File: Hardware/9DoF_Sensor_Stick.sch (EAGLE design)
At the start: 27 parts, among them U1 ITG-32001:1, U2 ADXL345, U4 3.3V

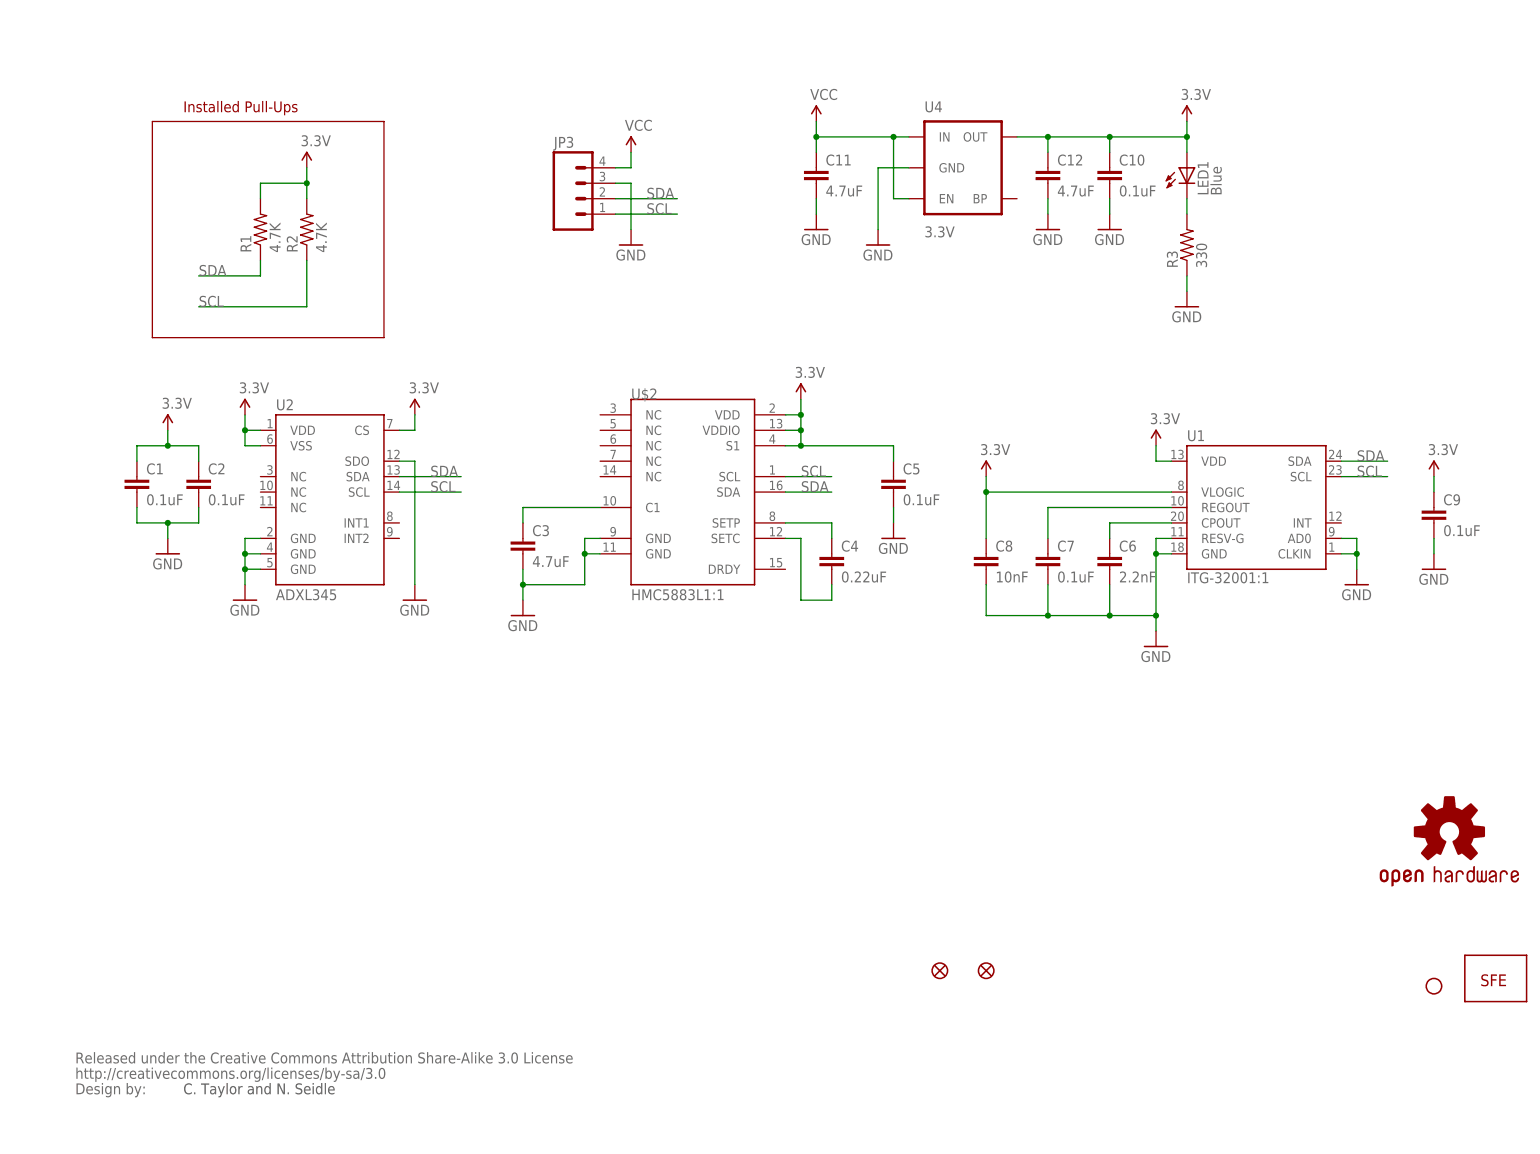
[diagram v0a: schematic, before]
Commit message: 2.0 Changes
- Replaces all three 3-axis sensors with single chip solution (LSM9DS1).
- Reduced board length from 1.3" to 1.0"
- ±2/±4/±8/±16 g linear acceleration full scale
- ±4/±8/±12/±16 gauss magnetic full scale
- ±245/±500/±2000 dps angular rate full scale
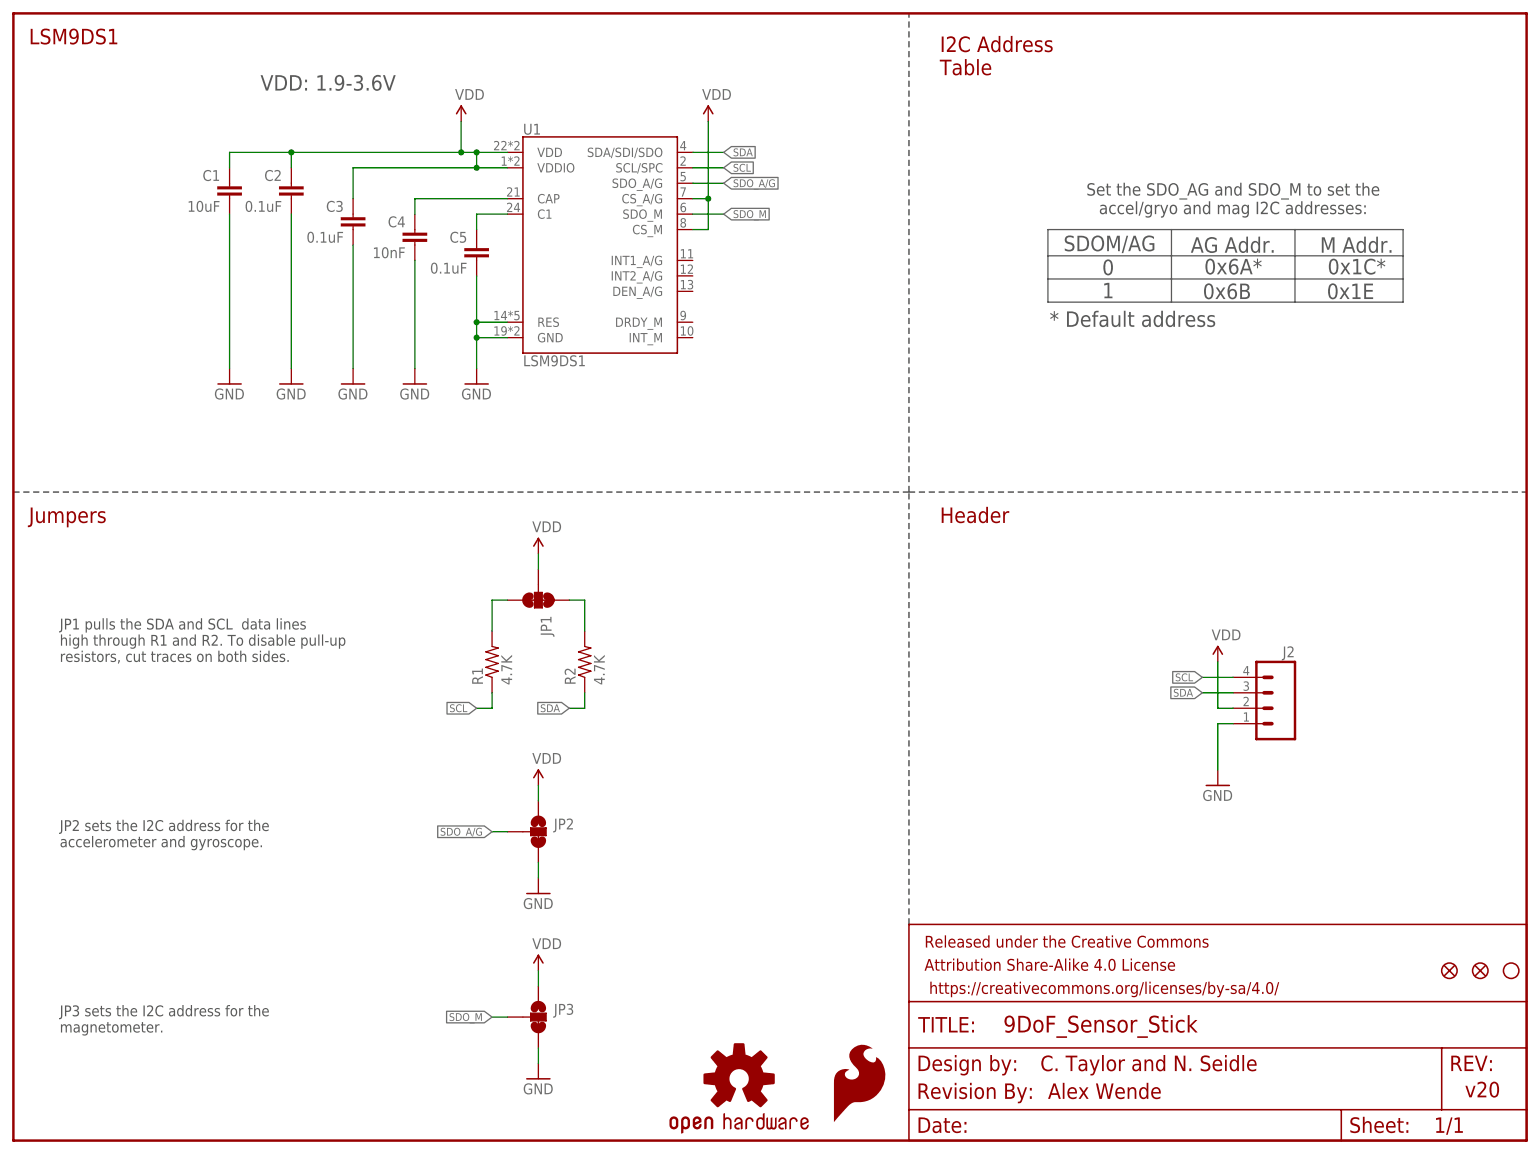
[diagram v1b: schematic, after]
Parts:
- removed C10, C7, C9: 0.1uF, SparkFun:CAP0402-CAP
- removed C11, C12: 4.7uF, SparkFun:CAP0402-CAP
- removed C6: 2.2nF, SparkFun:CAP0402-CAP
- removed C8: 10nF, SparkFun:CAP0402-CAP
- removed JP4: LOGO-SFESK, SparkFun:LOGO-SFESK
- removed JP5: STAND-OFF, SparkFun:STAND-OFF
- removed LED1: Blue, SparkFun:LED0603
- removed R3: 330, SparkFun:RESISTOR0402-RES
- removed U$2: HMC5883L1:1, Testing:HMC5883L1:1
- removed U$3: OSHW-LOGOS, SparkFun:OSHW-LOGOS
- removed U2: ADXL345, SparkFun:ADXL345
- removed U4: 3.3V, SparkFun:V_REG_LDOSMD
- added FD1, FD2: FIDUCIAL1X2, SparkFun-Aesthetics:FIDUCIAL1X2
- added FRAME1: FRAME-LETTER, SparkFun-Aesthetics:FRAME-LETTER
- added H1: STAND-OFF, SparkFun-Electromechanical:STAND-OFF
- added J2: (no value), SparkFun-Connectors:M04NO_SILK_ALL_ROUND
- added LOGO1: SFE_LOGO_FLAME.1_INCH, SparkFun-Aesthetics:SFE_LOGO_FLAME.1_INCH
- added LOGO3: OSHW-LOGOMINI, SparkFun-Aesthetics:OSHW-LOGOMINI
- C1: value 0.1uF -> 10uF; device SparkFun:CAP0402-CAP -> SparkFun-Capacitors:10UF-6.3V-20%(0603)
- C2, C5: device SparkFun:CAP0402-CAP -> SparkFun-Capacitors:0.1UF-25V(+80/-20%)(0603)
- C3: value 4.7uF -> 0.1uF; device SparkFun:CAP0402-CAP -> SparkFun-Capacitors:0.1UF-25V(+80/-20%)(0603)
- C4: value 0.22uF -> 10nF; device SparkFun:CAP0402-CAP -> SparkFun-Capacitors:10NF/10000PF-50V-10%(0603)
- JP1: value FIDUCIAL1X2 -> (none); device SparkFun:FIDUCIAL1X2 -> SparkFun-Passives:JUMPER-PAD-3-NC_BY_TRACE
- JP2: value FIDUCIAL1X2 -> JUMPER-PAD-3-2OF3_NC_BY_TRACE_SMALL; device SparkFun:FIDUCIAL1X2 -> SparkFun-Passives:JUMPER-PAD-3-2OF3_NC_BY_TRACE_SMALL
- JP3: value (none) -> JUMPER-PAD-3-2OF3_NC_BY_TRACE_SMALL; device SparkFun:M04PTH -> SparkFun-Passives:JUMPER-PAD-3-2OF3_NC_BY_TRACE_SMALL
- R1, R2: device SparkFun:RESISTOR0402-RES -> SparkFun-Resistors:4.7KOHM-1/10W-1%(0603)
- U$1: value CREATIVE_COMMONS -> REVISION; device SparkFun:CREATIVE_COMMONS -> SparkFun-Aesthetics:REVISION
- U1: value ITG-32001:1 -> LSM9DS1; device Testing:ITG-32001:1 -> SparkFun-Sensors:LSM9DS1
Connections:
- removed net 3.3V: C1.1, C10.1, C12.1, C2.1, C5.1, C8.1, C9.1, LED1.A, R1.2, R2.2, U$2.S1, U$2.VDD, U$2.VDDIO, U1.VDD, U1.VLOGIC, U2.CS, U2.VDD, U2.VSS, U4.OUT
- removed net N$3: C4.2, U$2.SETC
- removed net N$4: LED1.C, R3.2
- removed net N$7: C7.1, U1.REGOUT
- removed net VCC: C11.1, JP3.4, U4.EN, U4.IN
- new net N$6: C5.1, U1.C1
- new net SDO_A/G: JP2.2, U1.SDO_A/G
- new net SDO_M: JP3.2, U1.SDO_M
- new net VDD: C1.1, C2.1, C3.1, J2.2, JP1.2, JP2.1, JP3.1, U1.CS_A/G, U1.CS_M, U1.VDD, U1.VDDIO
- net GND: now also C4.2, J2.1, JP2.3, U1.RES; no longer C10.2, C11.2, C12.2, C6.2, C7.2, C8.2, C9.2, R3.1, U$2.GND@1, U$2.GND@2, U1.AD0, U1.CLKIN, U1.RESV-G, U2.GND@2, U2.GND@4, U2.GND@5, U2.SDO, U4.GND
- net N$1: now also JP1.1, R2.2; no longer C3.1, U$2.C1
- net N$2: now also JP1.3, R1.2; no longer C4.1, U$2.SETP
- net N$5: now also C4.1, U1.CAP; no longer C6.1, U1.CPOUT
- net SCL: now also J2.4, R1.1, U1.SCL/SPC; no longer JP3.1, R2.1, U$2.SCL, U1.SCL, U2.SCL
- net SDA: now also J2.3, R2.1, U1.SDA/SDI/SDO; no longer JP3.2, R1.1, U$2.SDA, U1.SDA, U2.SDA
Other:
- note added: "* Default address"
- note added: "0 1"
- note added: "0x1C*"
- note added: "0x1E"
- note added: "0x6A*"
- note added: "0x6B"
- note added: "AG Addr."
- note added: "Alex Wende"
- note added: "Header"
- note added: "I2C Address Table"
- note added: "JP1 pulls the SDA and SCL data lines high through R1 and R2. To disable pull-up resistors, cut traces on both sides."
- note added: "JP2 sets the I2C address for the accelerometer and gyroscope."
- note added: "JP3 sets the I2C address for the magnetometer."
- note added: "Jumpers"
- note added: "LSM9DS1"
- note added: "M Addr."
- note added: "SDOM/AG"
- note added: "Set the SDO_AG and SDO_M to set the accel/gryo and mag I2C addresses:"
- note added: "VDD: 1.9-3.6V"
- note added: "v20"
- note removed: "Installed Pull-Ups"
- moved on the sheet: C1, C2, C3, C4, C5, R1, R2

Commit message: v20 Changes
- Switch to micro fiducials for better clearances.
- Changed default I2C addresses to ox1E and 0x6B to match example code
for LSM9DS1 Breakout.
- Moved "v20" bottom copper text to clear bottom silk
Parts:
- removed FD1, FD2: FIDUCIAL1X2, SparkFun-Aesthetics:FIDUCIAL1X2
- removed U$1: REVISION, SparkFun-Aesthetics:REVISION
- added FD3, FD4: FIDUCIALUFIDUCIAL, SparkFun-Aesthetics:FIDUCIALUFIDUCIAL
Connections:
- net GND: now also JP2.1, JP3.1; no longer JP2.3, JP3.3
- net VDD: now also JP2.3, JP3.3; no longer JP2.1, JP3.1
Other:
- note added: "0x1C"
- note added: "0x1E*"
- note added: "0x6A"
- note added: "0x6B*"
- note removed: "0x1C*"
- note removed: "0x1E"
- note removed: "0x6A*"
- note removed: "0x6B"
- note removed: "C. Taylor and N. Seidle"
- moved on the sheet: JP2, JP3
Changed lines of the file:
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@@
 <parts>
 <part name="FRAME1" library="SparkFun-Aesthetics" deviceset="FRAME-LETTER" device=""/>
-<part name="U$1" library="SparkFun-Aesthetics" deviceset="REVISION" device=""/>
 <part name="U1" library="SparkFun-Sensors" deviceset="LSM9DS1" device=""/>
 <part name="SUPPLY1" library="SparkFun-Aesthetics" deviceset="VDD" device=""/>
@@
 <part name="SUPPLY3" library="SparkFun-Aesthetics" deviceset="VDD" device=""/>
 <part name="GND6" library="SparkFun-Aesthetics" deviceset="GND" device=""/>
-<part name="FD1" library="SparkFun-Aesthetics" deviceset="FIDUCIAL" device="1X2"/>
-<part name="FD2" library="SparkFun-Aesthetics" deviceset="FIDUCIAL" device="1X2"/>
 <part name="H1" library="SparkFun-Electromechanical" deviceset="STAND-OFF" device=""/>
 <part name="LOGO1" library="SparkFun-Aesthetics" deviceset="SFE_LOGO_FLAME" device=".1_INCH"/>
@@
 <part name="SUPPLY6" library="SparkFun-Aesthetics" deviceset="VDD" device=""/>
 <part name="GND8" library="SparkFun-Aesthetics" deviceset="GND" device=""/>
+<part name="FD3" library="SparkFun-Aesthetics" deviceset="FIDUCIAL" device="UFIDUCIAL"/>
+<part name="FD4" library="SparkFun-Aesthetics" deviceset="FIDUCIAL" device="UFIDUCIAL"/>
 </parts>
 <sheets>
 <sheet>
 <plain>
-<text x="168.91" y="11.43" size="2.54" layer="94">C. Taylor and N. Seidle</text>
-<text x="170.18" y="6.858" size="2.54" layer="94">Alex Wende</text>
+<text x="167.132" y="11.43" size="2.54" layer="94">Alex Wende</text>
 <text x="238.76" y="7.112" size="2.54" layer="94">v20</text>
 <text x="2.54" y="180.34" size="2.54" layer="94">LSM9DS1</text>
@@
 <text x="7.62" y="17.78" size="1.778" layer="97">JP3 sets the I2C address for the
 magnetometer.</text>
-<text x="200.66" y="143.764" size="2.54" layer="97" align="center">0x6A*</text>
-<text x="199.644" y="139.7" size="2.54" layer="97" align="center">0x6B</text>
-<text x="220.98" y="143.764" size="2.54" layer="97" align="center">0x1C*</text>
-<text x="219.964" y="139.7" size="2.54" layer="97" align="center">0x1E</text>
+<text x="199.644" y="143.764" size="2.54" layer="97" align="center">0x6A</text>
+<text x="200.66" y="139.7" size="2.54" layer="97" align="center">0x6B*</text>
+<text x="220.726" y="143.764" size="2.54" layer="97" align="center">0x1C</text>
+<text x="221.742" y="139.7" size="2.54" layer="97" align="center">0x1E*</text>
 <text x="184.15" y="135.128" size="2.54" layer="97" align="center">* Default address</text>
 <text x="40.64" y="172.72" size="2.54" layer="97">VDD: 1.9-3.6V</text>
@@
 <instance part="FRAME1" gate="G$1" x="0" y="0"/>
 <instance part="FRAME1" gate="V" x="147.32" y="0"/>
-<instance part="U$1" gate="G$1" x="148.59" y="6.858"/>
 <instance part="U1" gate="G$1" x="96.52" y="147.32"/>
 <instance part="SUPPLY1" gate="VDD" x="73.66" y="167.64"/>
@@
 <instance part="SUPPLY3" gate="VDD" x="198.12" y="78.74"/>
 <instance part="GND6" gate="1" x="198.12" y="58.42"/>
-<instance part="FD1" gate="G$1" x="241.3" y="27.94"/>
-<instance part="FD2" gate="G$1" x="236.22" y="27.94"/>
 <instance part="H1" gate="G$1" x="246.38" y="27.94"/>
 <instance part="LOGO1" gate="G$1" x="134.62" y="2.54"/>
 <instance part="LOGO3" gate="G$1" x="119.38" y="10.16"/>
 <instance part="SUPPLY4" gate="VDD" x="114.3" y="167.64"/>
-<instance part="JP2" gate="G$1" x="86.36" y="50.8"/>
+<instance part="JP2" gate="G$1" x="86.36" y="50.8" rot="MR180"/>
 <instance part="SUPPLY5" gate="VDD" x="86.36" y="58.42"/>
 <instance part="GND7" gate="1" x="86.36" y="40.64"/>
-<instance part="JP3" gate="G$1" x="86.36" y="20.32"/>
+<instance part="JP3" gate="G$1" x="86.36" y="20.32" rot="MR180"/>
 <instance part="SUPPLY6" gate="VDD" x="86.36" y="27.94"/>
 <instance part="GND8" gate="1" x="86.36" y="10.16"/>
+<instance part="FD3" gate="G$1" x="241.3" y="27.94"/>
+<instance part="FD4" gate="G$1" x="236.22" y="27.94"/>
 </instances>
 <busses>
@@
 </segment>
 <segment>
-<pinref part="JP2" gate="G$1" pin="1"/>
-<wire x1="86.36" y1="55.88" x2="86.36" y2="58.42" width="0.1524" layer="91"/>
 <pinref part="SUPPLY5" gate="VDD" pin="VDD"/>
-</segment>
-<segment>
-<pinref part="JP3" gate="G$1" pin="1"/>
+<pinref part="JP2" gate="G$1" pin="3"/>
+<wire x1="86.36" y1="58.42" x2="86.36" y2="55.88" width="0.1524" layer="91"/>
+</segment>
+<segment>
+<pinref part="JP3" gate="G$1" pin="3"/>
+<pinref part="SUPPLY6" gate="VDD" pin="VDD"/>
 <wire x1="86.36" y1="25.4" x2="86.36" y2="27.94" width="0.1524" layer="91"/>
-<pinref part="SUPPLY6" gate="VDD" pin="VDD"/>
 </segment>
 </net>
@@
 </segment>
 <segment>
-<pinref part="JP2" gate="G$1" pin="3"/>
+<pinref part="JP2" gate="G$1" pin="1"/>
+<pinref part="GND7" gate="1" pin="GND"/>
 <wire x1="86.36" y1="45.72" x2="86.36" y2="43.18" width="0.1524" layer="91"/>
-<pinref part="GND7" gate="1" pin="GND"/>
-</segment>
-<segment>
-<pinref part="JP3" gate="G$1" pin="3"/>
+</segment>
+<segment>
+<pinref part="JP3" gate="G$1" pin="1"/>
+<pinref part="GND8" gate="1" pin="GND"/>
 <wire x1="86.36" y1="15.24" x2="86.36" y2="12.7" width="0.1524" layer="91"/>
-<pinref part="GND8" gate="1" pin="GND"/>
-</segment>
-</net>
+</segment>
+</net>

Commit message: V21 Changes
Changes since initial v20:
- Switched to micro fiducials for better clearances
- Changed default I2C addresses to 0x1E and 0x6B to match LSM9DS1
breakout board example code
- Moved version text on bottom copper to clear the bottom silk
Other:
- note added: "v21"
- note removed: "v20"
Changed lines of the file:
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@@
 <plain>
 <text x="167.132" y="11.43" size="2.54" layer="94">Alex Wende</text>
-<text x="238.76" y="7.112" size="2.54" layer="94">v20</text>
+<text x="238.76" y="7.112" size="2.54" layer="94">v21</text>
 <text x="2.54" y="180.34" size="2.54" layer="94">LSM9DS1</text>
 <wire x1="147.32" y1="35.56" x2="147.32" y2="106.68" width="0.254" layer="97" style="longdash"/>
